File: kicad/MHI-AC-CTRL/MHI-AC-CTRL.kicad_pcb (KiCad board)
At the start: 2 copper layers, 51.6 x 26.8 mm, 8 parts, among them J1 Conn_01x05, U1 TSR_1-2450, U2 ESP-C3-32S-Kit, U3 LEVEL-SHIFTER-4CH

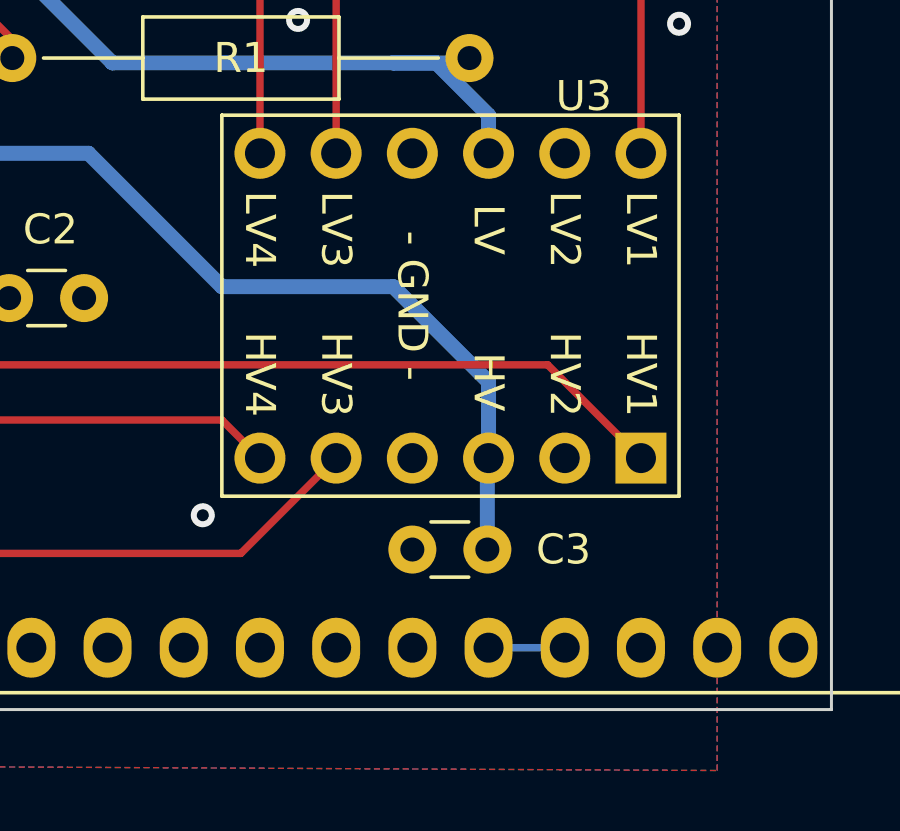
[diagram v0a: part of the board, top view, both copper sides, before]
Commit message: Remove SPI loopback from PCB
Only removed the loopback signal and upgraded KiCad. Did not order the
new version myself.

After commit 99ec16f (Remove physical CS loopback requirement,
2026-03-19), we don't need the CS loopback any more
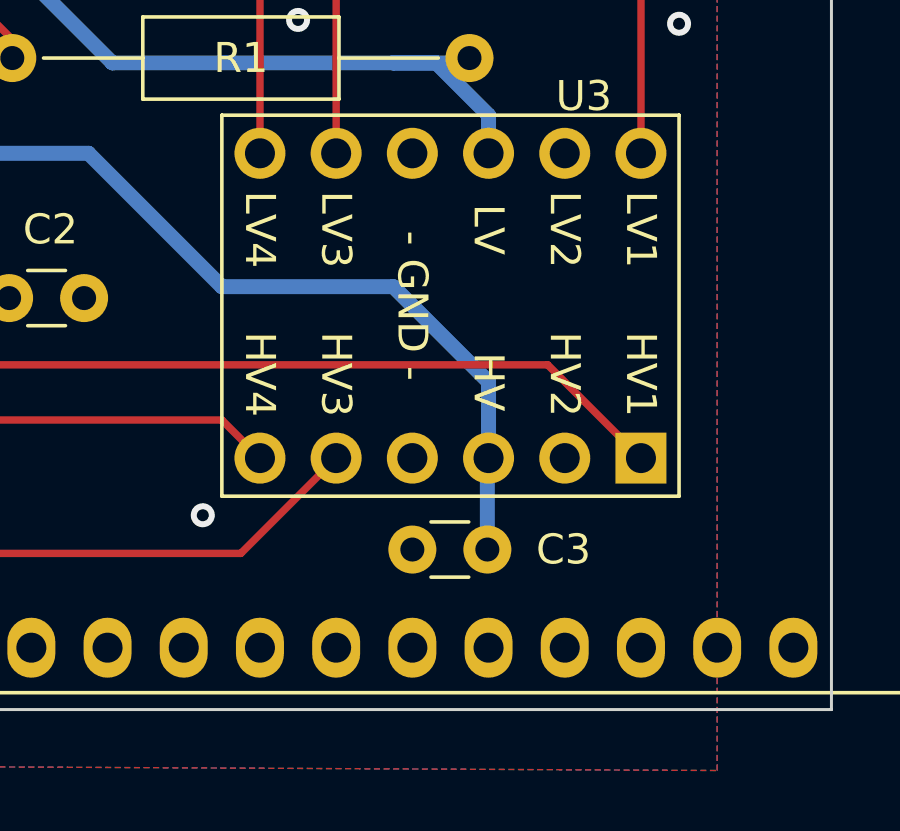
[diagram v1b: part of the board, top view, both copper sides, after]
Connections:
- U2 pad 26: Net-(U2-IO10) -> unconnected-(U2-IO10-Pad26)
- U2 pad 27: Net-(U2-IO10) -> unconnected-(U2-IO9-Pad27)
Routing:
- net Net-(U2-IO10): track 2.54 -> 0.00 mm
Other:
- board text added: "MHI-AC-Ctrl-ESP32-C3 v1.1 March 2026"
- board text removed: "MHI-AC-Ctrl-ESP32-C3 v1.0 January 2023"
